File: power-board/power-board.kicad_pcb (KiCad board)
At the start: 2 copper layers, 100 x 100 mm, 41 parts, among them J1 USB_C, J2 Conn_01x02, J3 Conn_01x02, J4 Conn_01x02, J5 Bat+, J6 Conn_01x03, J7 Bat-, Q1 AOB2146L, Q2 AOB2146L, SW1 On, SW2 Mode, U1 AP9101CK6, U2 AP130-33Y, U3 MCP73831-3-OT, U4 ESP8266-NodeM

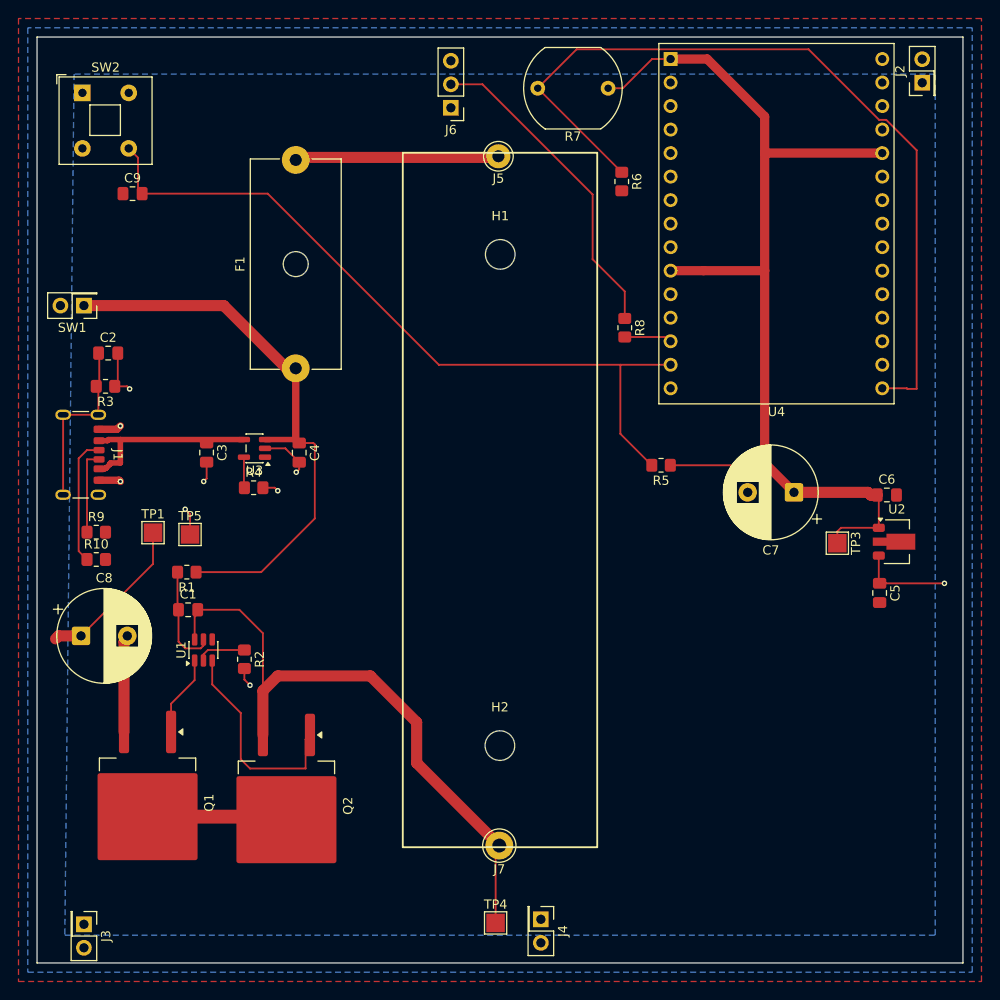
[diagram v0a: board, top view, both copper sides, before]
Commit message: inrush limiting / soft start & orientation of dev board
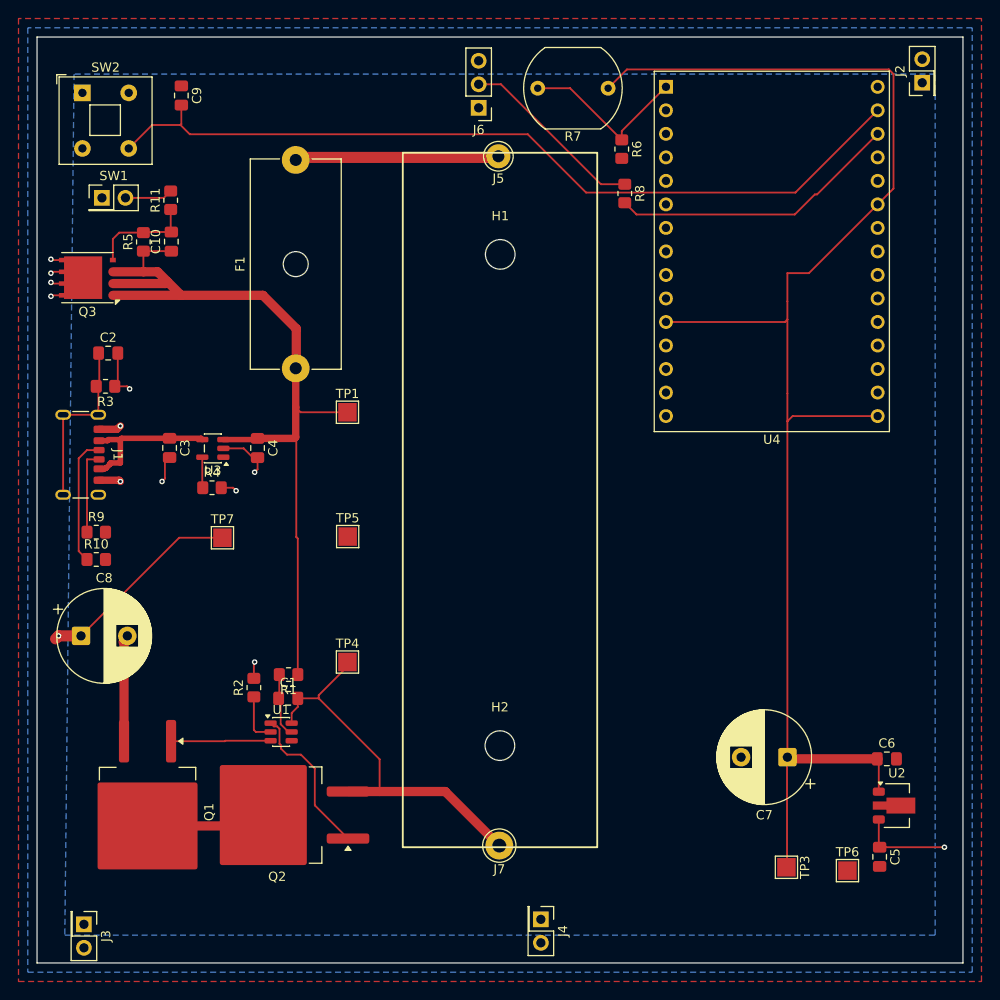
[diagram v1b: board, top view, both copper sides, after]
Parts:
- added C10: 1u, Capacitor_SMD:C_0805_2012Metric_Pad1.18x1.45mm_HandSolder, F.Cu at (64.5, 72.1)
- added Q3: AON7407, Package_DFN_QFN:AO_DFN-8-1EP_5.55x5.2mm_P1.27mm_EP4.12x4.6mm, F.Cu at (55.4, 76.0)
- added R11: 10k, Resistor_SMD:R_0805_2012Metric_Pad1.20x1.40mm_HandSolder, F.Cu at (64.4, 67.6)
- added TP6: Gnd, TestPoint:TestPoint_Pad_2.0x2.0mm, F.Cu at (137.5, 140.0)
- added TP7: VSW, TestPoint:TestPoint_Pad_2.0x2.0mm, F.Cu at (70.0, 104.1)
- R5: value 10k -> 100k
- U1: value AP9101CK6 -> AP9101CAK6
- moved R5 60.9 mm to (61.5, 72.1), turned to 90 degrees
- moved TP3 35.4 mm to (130.9, 139.7)
- moved TP4 32.4 mm to (83.5, 117.5)
- moved C7 28.6 mm to (131.0, 127.8)
- moved C5 28.5 mm to (141.0, 138.5)
- moved C6 28.5 mm to (141.8, 128.0)
- moved U2 28.5 mm to (142.9, 133.0)
- moved TP1 24.7 mm to (83.5, 90.5)
- moved TP5 17.0 mm to (83.5, 104.0)
- moved R1 15.6 mm to (77.2, 118.9)
- moved R8 14.5 mm to (113.5, 66.9)
- moved C1 14.4 mm to (77.1, 121.4)
- moved U1 12.2 mm to (76.4, 125.0), turned to 0 degrees
- moved C9 11.8 mm to (65.6, 56.3), turned to -90 degrees
- moved SW1 11.8 mm to (57.0, 67.4), turned to 0 degrees
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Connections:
- C4 pad 1: Net-(SW1-A) -> +BATT
- F1 pad 1: Net-(SW1-A) -> +BATT
- R1 pad 1: Net-(SW1-A) -> +BATT
- R5 pad 1: +3V3 -> +BATT
- R5 pad 2: Net-(SW2-A) -> Net-(Q3-G)
- R6 pad 1: Net-(U4-A0) -> Net-(R6-Pad1)
- R7 pad 2: Net-(U4-A0) -> Net-(R6-Pad1)
- SW1 pad 1: Net-(SW1-A) -> GND
- SW1 pad 2: +VSW -> Net-(SW1-B)
- TP1 pad 1: +VSW -> +BATT
- U1 pad 1: Net-(Q1-G) -> Net-(Q2-G)
- U1 pad 3: Net-(Q2-G) -> Net-(Q1-G)
- U3 pad 3: Net-(SW1-A) -> +BATT
- U4 pad 1: +3V3 -> Net-(R6-Pad1)
- U4 pad 10: +3V3 -> GND
- U4 pad 11: unconnected-(U4-Pad11) -> +3V3
- U4 pad 13: Net-(U4-D2) -> unconnected-(U4-Pad13)
- U4 pad 14: Net-(SW2-A) -> GND
- U4 pad 16: Net-(U4-A0) -> +3V3
- U4 pad 17: unconnected-(U4-Pad17) -> GND
- U4 pad 2: GND -> unconnected-(U4-Pad2)
- U4 pad 24: unconnected-(U4-Pad24) -> GND
- U4 pad 25: GND -> +3V3
- U4 pad 26: +3V3 -> unconnected-(U4-Pad26)
- U4 pad 28: unconnected-(U4-Pad28) -> Net-(U4-D2)
- U4 pad 29: GND -> Net-(SW2-A)
- U4 pad 9: GND -> unconnected-(U4-Pad9)
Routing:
- net +BATT: track 0.00 -> 92.5 mm
- net Net-(U4-A0): track 89.5 -> 0.00 mm
- net Net-(SW1-A): track 62.7 -> 0.00 mm
- net +3V3: track 114.5 -> 160.6 mm
- net Net-(U4-D2): track 5.14 -> 31.4 mm
- net /BAT-: track 67.3 -> 42.0 mm
- net Net-(R6-Pad1): track 0.00 -> 19.1 mm
- net Net-(J6-Pin_2): track 35.1 -> 20.2 mm
- net Net-(Q3-G): track 0.00 -> 11.4 mm
- net +VSW: track 27.3 -> 37.3 mm, vias 1 -> 6
- net Net-(SW2-A): track 82.5 -> 90.8 mm
- net Net-(Q2-G): track 23.2 -> 17.0 mm
- net Net-(SW1-B): track 0.00 -> 5.19 mm
- net Net-(U3-V_{DD}): track 20.8 -> 16.4 mm
- net Net-(U1-VDD): track 11.3 -> 7.02 mm
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
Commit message: tracks layout
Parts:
- moved C2 22.0 mm to (60.9, 105.9), turned to 180 degrees
- moved R3 16.0 mm to (60.8, 103.3), turned to 0 degrees
- moved C9 13.6 mm to (67.1, 69.8), turned to 0 degrees
- moved R11 5.88 mm to (67.2, 72.8), turned to 180 degrees
- moved R5 5.75 mm to (65.5, 76.3)
- moved Q3 5.68 mm to (56.2, 81.6)
- moved C10 5.60 mm to (68.2, 76.3)
- moved SW1 5.58 mm to (55.5, 72.8)
- moved R1 4.49 mm to (81.7, 118.9)
- moved C1 4.46 mm to (81.6, 121.4)
- moved TP4 4.32 mm to (86.0, 121.0)
- moved U1 4.27 mm to (80.6, 125.2)
- moved R2 4.02 mm to (77.3, 121.4), turned to 180 degrees
- moved TP5 3.22 mm to (86.2, 105.8)
- moved TP1 2.72 mm to (86.2, 91.2)
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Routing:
- net +BATT: track 92.5 -> 43.9 mm
- net /BAT-: track 42.0 -> 17.4 mm
- net GND: track 33.8 -> 10.4 mm, vias 7 -> 17
- net Net-(J5-Pin_1): track 22.1 -> 0.00 mm
- net Net-(J1-SHIELD): track 19.3 -> 10.2 mm
- net Net-(Q1-G): track 10.8 -> 16.3 mm
- net Net-(R6-Pad1): track 19.1 -> 23.1 mm
- net Net-(SW1-B): track 5.19 -> 8.14 mm
- net Net-(Q3-G): track 11.4 -> 14.3 mm
- net +3V3: track 160.6 -> 163.2 mm
- net Net-(SW2-A): track 90.8 -> 92.9 mm
- net +VSW: track 37.3 -> 35.3 mm, vias 6 -> 9
- net Net-(Q1-D): track 16.8 -> 14.8 mm
- net Net-(U4-D2): track 31.4 -> 32.6 mm
- net Net-(U1-VM): track 5.47 -> 4.68 mm
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- added copper zone on F.Cu, net +BATT
- added copper zone on F.Cu, net +VSW
- added copper zone on F.Cu, net /BAT-
- added copper zone on F.Cu, net Net-(J5-Pin_1)

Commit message: v1
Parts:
- J2: value Conn_01x02 -> - +
- J3, J4: value Conn_01x02 -> + -
- J6: value Conn_01x03 -> - In +
- moved R6 0.50 mm to (113.0, 62.1)
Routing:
- net Net-(J1-CC1): track 13.4 -> 13.9 mm
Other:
- outline, holes or cut-outs redrawn
- board text added: "RGB matrix wifi 18650 cell"
- board text added: "kaleidoscope jpsecher 2026 v1"
